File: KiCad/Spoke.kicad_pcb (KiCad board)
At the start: 2 copper layers, 50 x 100 mm, 134 parts, among them J1 B2B-PH-K-S, J10 BL-A, J11 BL-C, J12 Amphenol 132289, J2 BAT+, J3 BAT-, J4 GCT USB4105/USB4110, J5 USB+, J6 USB-, J7 PLS-1x3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

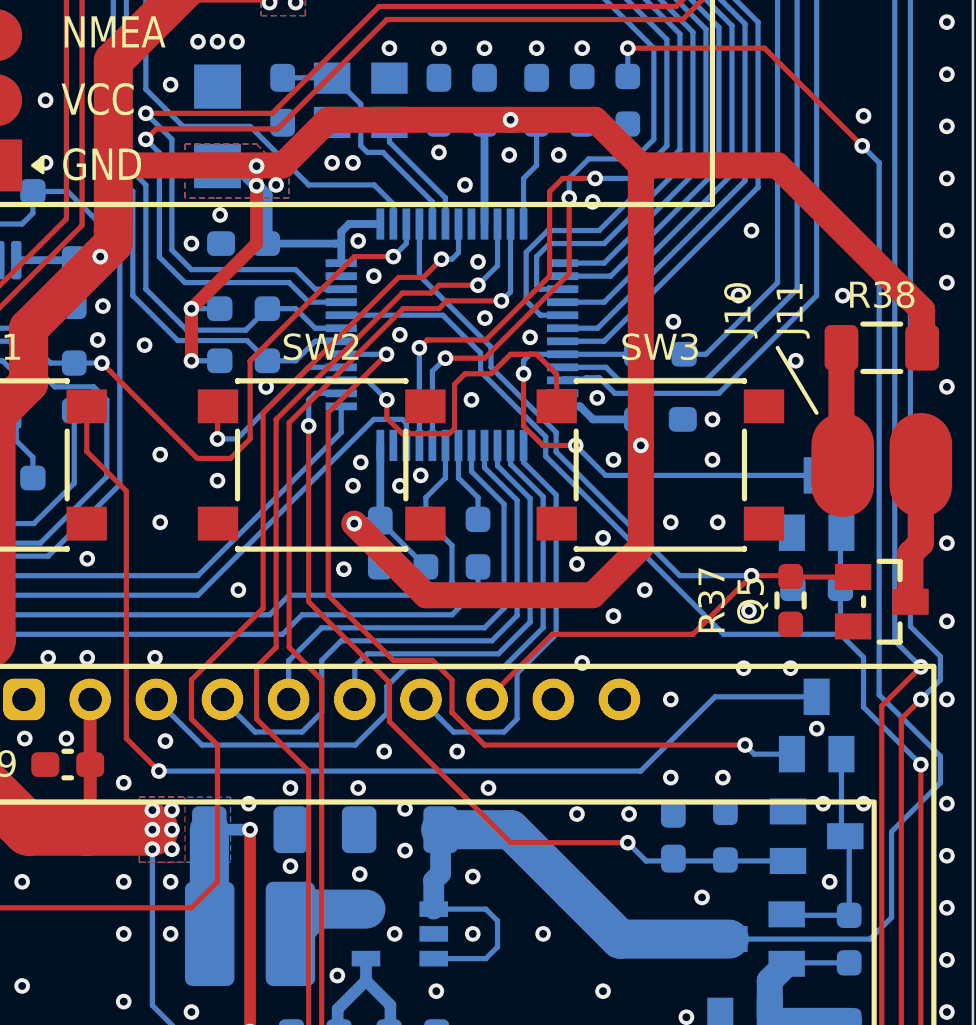
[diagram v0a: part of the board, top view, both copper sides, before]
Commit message: Swap PWR_HOLD and RF_TXEN; re-route
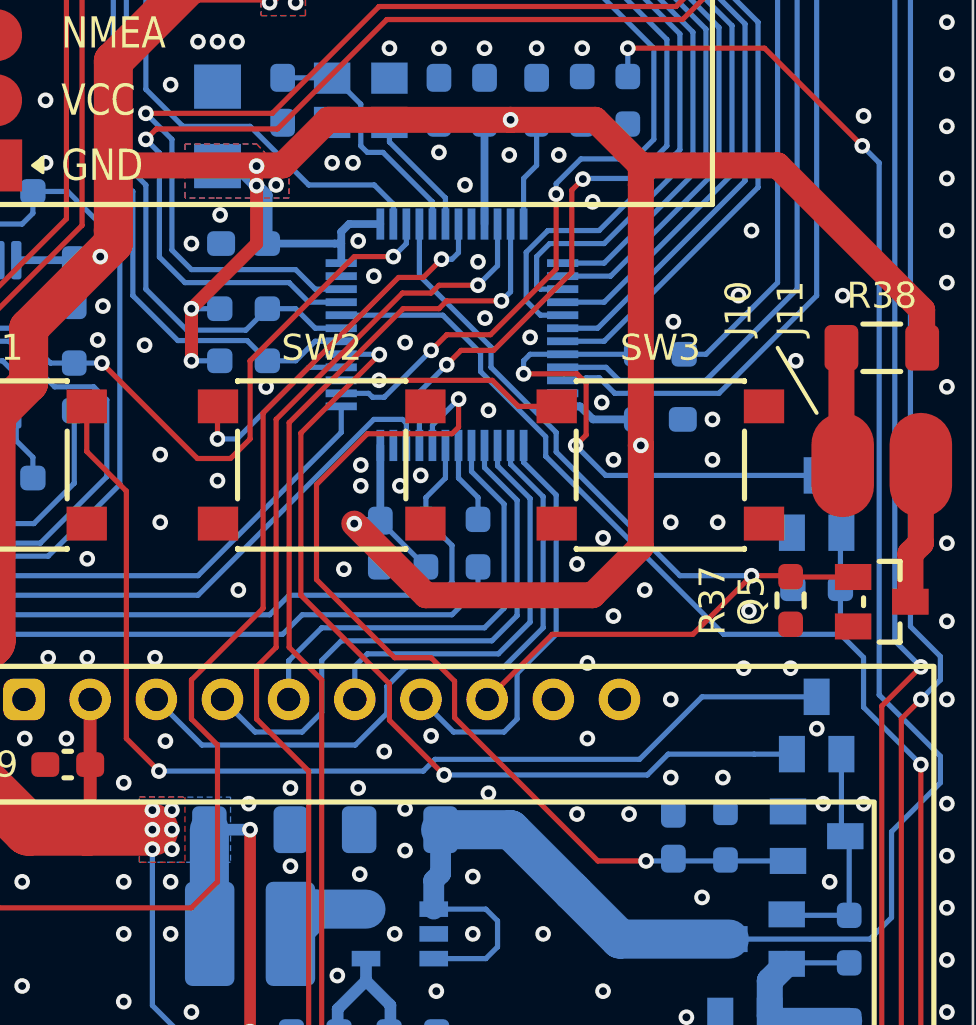
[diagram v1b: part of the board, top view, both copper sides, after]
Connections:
- U6 pad 32: RF_TXEN -> PWR_HOLD
- U6 pad 38: PWR_HOLD -> RF_TXEN
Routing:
- net BTN_ESC: track 13.3 -> 8.68 mm
- net PWR_HOLD: track 32.5 -> 36.7 mm
- net BTN_PWR: track 33.0 -> 34.8 mm
- net RF_RXEN: track 37.6 -> 36.6 mm
- net RF_TXEN: track 36.9 -> 37.8 mm
- net PPS_BOOT1: track 19.0 -> 19.8 mm
- net GND: vias 427 -> 428

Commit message: Improve PPS_BOOT1 routing
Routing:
- net PPS_BOOT1: track 19.8 -> 14.3 mm
- net GND: vias 428 -> 432
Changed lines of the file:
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@@
 	)
 	(via
+		(at 118.2 99)
+		(size 0.6)
+		(drill 0.3)
+		(layers "F.Cu" "B.Cu")
+		(free yes)
+		(net 1)
+	)
+	(via
 		(at 105 72.8)
 		(size 0.6)
@@
 	)
 	(via
-		(at 111.2 99.8)
+		(at 111 100)
 		(size 0.6)
 		(drill 0.3)
@@
 	)
 	(via
+		(at 118.8 97)
+		(size 0.6)
+		(drill 0.3)
+		(layers "F.Cu" "B.Cu")
+		(free yes)
+		(net 1)
+	)
+	(via
 		(at 100.4 88.4)
 		(size 0.6)
@@
 	)
 	(via
-		(at 113.5 94.5)
+		(at 113.6 93.6)
 		(size 0.6)
 		(drill 0.3)
@@
 	)
 	(via
-		(at 118.2 96)
+		(at 117.8 96)
 		(size 0.6)
 		(drill 0.3)
@@
 	)
 	(via
+		(at 110.1 99.2)
+		(size 0.6)
+		(drill 0.3)
+		(layers "F.Cu" "B.Cu")
+		(free yes)
+		(net 1)
+	)
+	(via
 		(at 110.751473 97.6)
 		(size 0.6)
@@
 	)
 	(via
+		(at 108 96.5)
+		(size 0.6)
+		(drill 0.3)
+		(layers "F.Cu" "B.Cu")
+		(free yes)
+		(net 1)
+	)
+	(via
 		(at 106.4 112.6)
 		(size 0.6)
@@
 	)
 	(segment
-		(start 110.150473 98.849527)
-		(end 109.75 99.25)
-		(width 0.2)
-		(layer "F.Cu")
-		(net 47)
-	)
-	(segment
-		(start 107.75 96.5)
-		(end 109.797 96.5)
+		(start 113.9 94.5)
+		(end 115.1 94.5)
 		(width 0.2)
 		(layer "F.Cu")
@@
 	)
 	(segment
-		(start 110.150473 96.853473)
-		(end 110.150473 98.849527)
-		(width 0.2)
-		(layer "F.Cu")
-		(net 47)
-	)
-	(segment
-		(start 109.797 96.5)
-		(end 110.150473 96.853473)
+		(start 115.1 94.5)
+		(end 117 96.4)
 		(width 0.2)
 		(layer "F.Cu")
@@
 	)
 	(via
-		(at 109.75 99.25)
+		(at 113.9 94.5)
 		(size 0.6)
 		(drill 0.3)
@@
 	)
 	(via
-		(at 107.75 96.5)
+		(at 117 96.4)
 		(size 0.6)
 		(drill 0.3)
@@
 	)
 	(segment
-		(start 109.75 99.25)
-		(end 110.9 100.4)
+		(start 109.25 95.75)
+		(end 112.0875 95.75)
 		(width 0.2)
 		(layer "B.Cu")
@@
 	)
 	(segment
-		(start 110.9 100.4)
-		(end 119 100.4)
+		(start 113.9 94.5)
+		(end 112.6 94.5)
 		(width 0.2)
 		(layer "B.Cu")
@@
 	)
 	(segment
-		(start 109.25 95.75)
-		(end 112.0875 95.75)
+		(start 112.6 94.5)
+		(end 112.0875 95.0125)
 		(width 0.2)
 		(layer "B.Cu")
@@
 	)
 	(segment
-		(start 108 95.75)
-		(end 109.25 95.75)
+		(start 119 100.4)
+		(end 119 98.4)
 		(width 0.2)
 		(layer "B.Cu")
@@
 	)
 	(segment
-		(start 107.75 96.5)
-		(end 107.75 96)
+		(start 119 98.4)
+		(end 117 96.4)
 		(width 0.2)
 		(layer "B.Cu")
@@
 	)
 	(segment
-		(start 107.75 96)
-		(end 108 95.75)
+		(start 112.0875 95.0125)
+		(end 112.0875 95.75)
 		(width 0.2)
 		(layer "B.Cu")

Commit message: Minor gloss
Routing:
- net GND: vias 432 -> 434

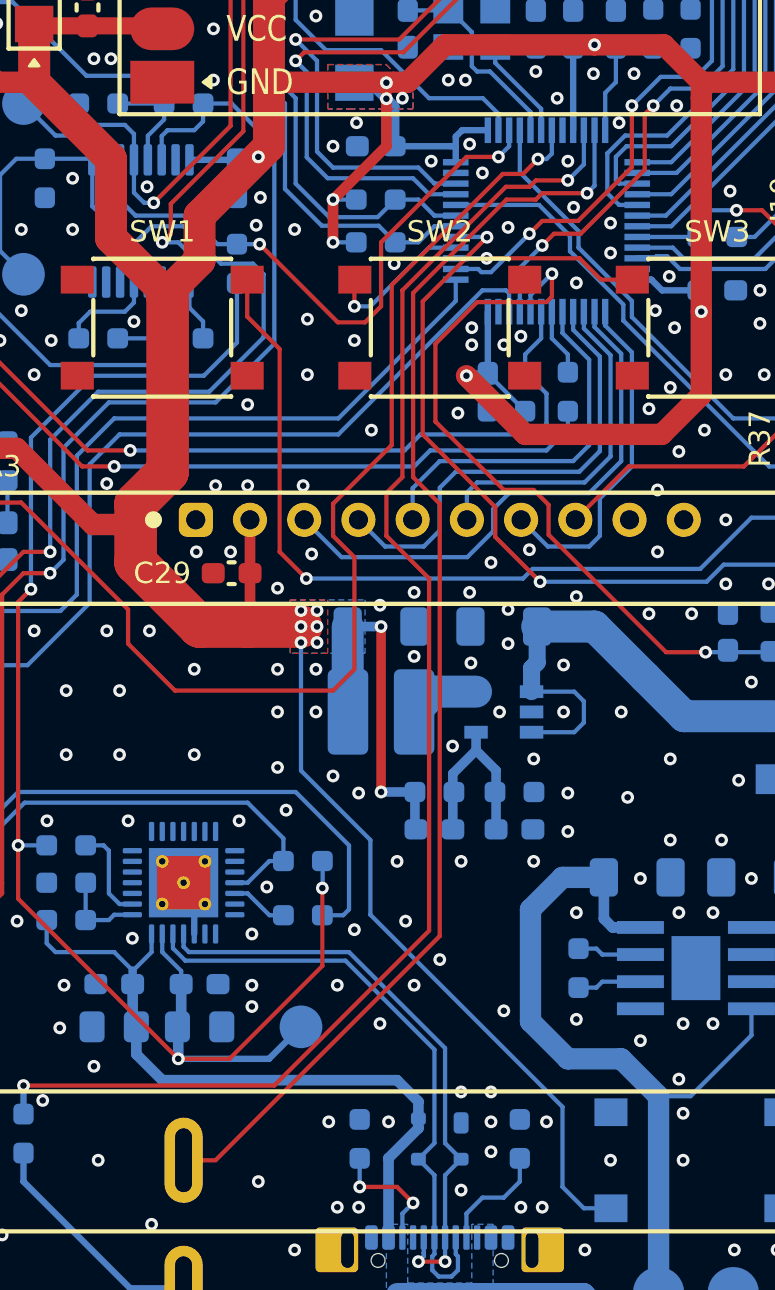
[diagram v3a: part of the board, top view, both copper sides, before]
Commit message: Move LCD_BL to PA1 (ex BUZZER_N)
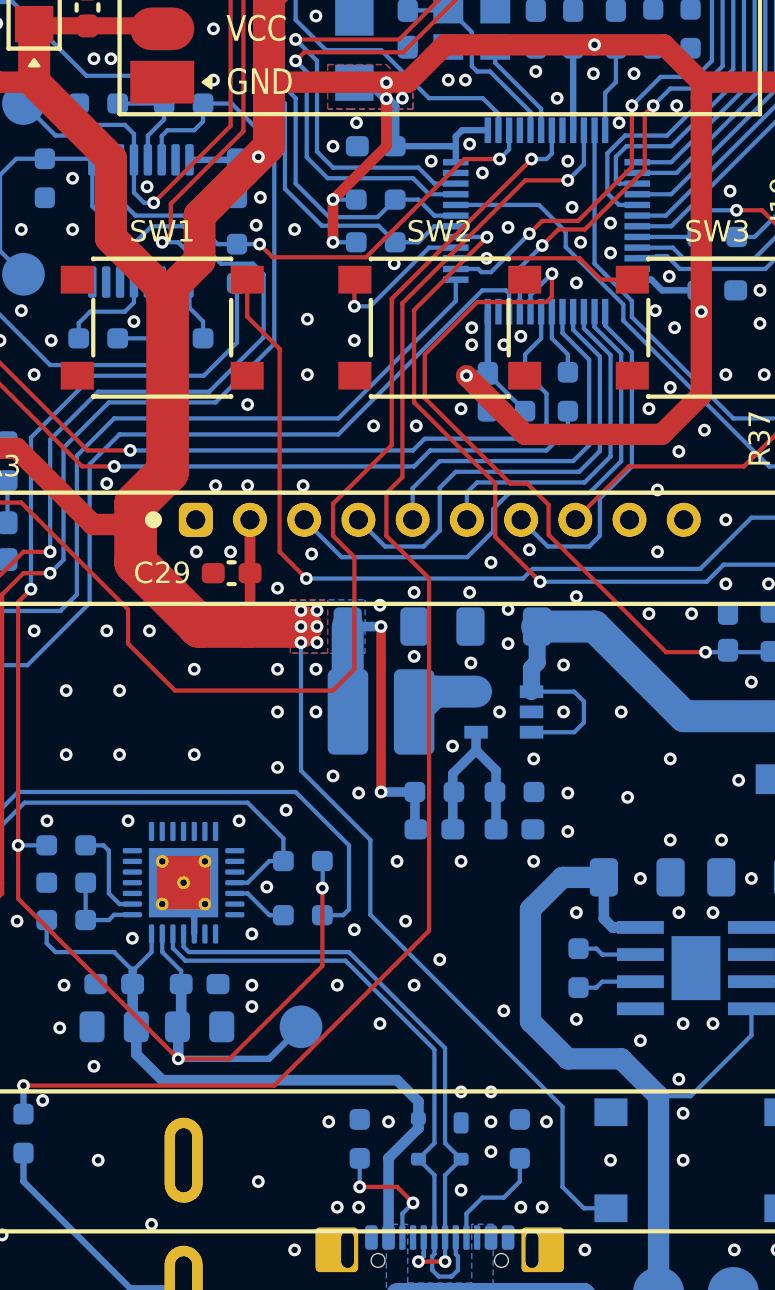
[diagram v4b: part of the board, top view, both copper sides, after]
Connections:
- net BUZZER_P renamed BUZZER
- LS1 pad 2: BUZZER_N -> unconnected-(LS1-Pad2)
- U6 pad 11: BUZZER_N -> LCD_BL
- U6 pad 4: LCD_BL -> unconnected-(U6-PC15-Pad4)
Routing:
- net BUZZER_N: track 60.2 -> 0.00 mm, vias 1 -> 0
- net MUX_BLE_USB: track 66.8 -> 62.6 mm
- net LCD_BL: track 36.4 -> 35.0 mm
- net GND: vias 434 -> 436

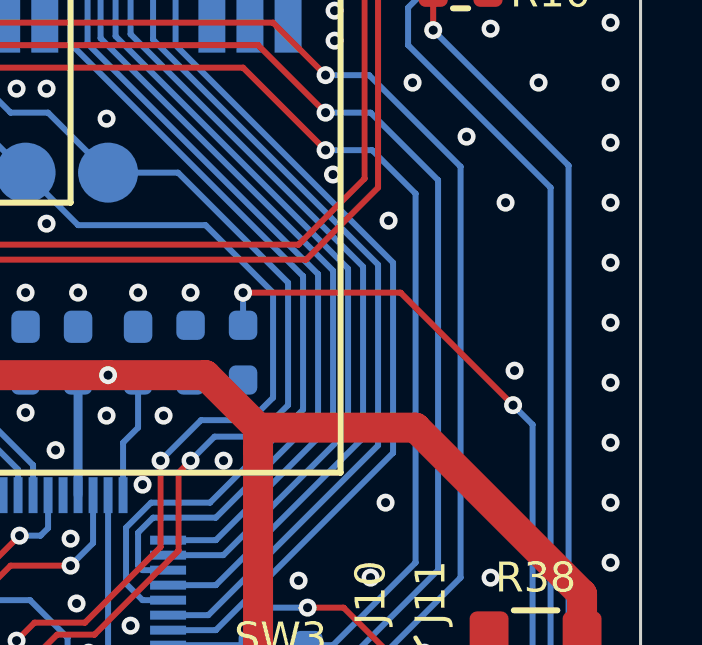
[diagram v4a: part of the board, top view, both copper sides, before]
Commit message: Add ALARM button
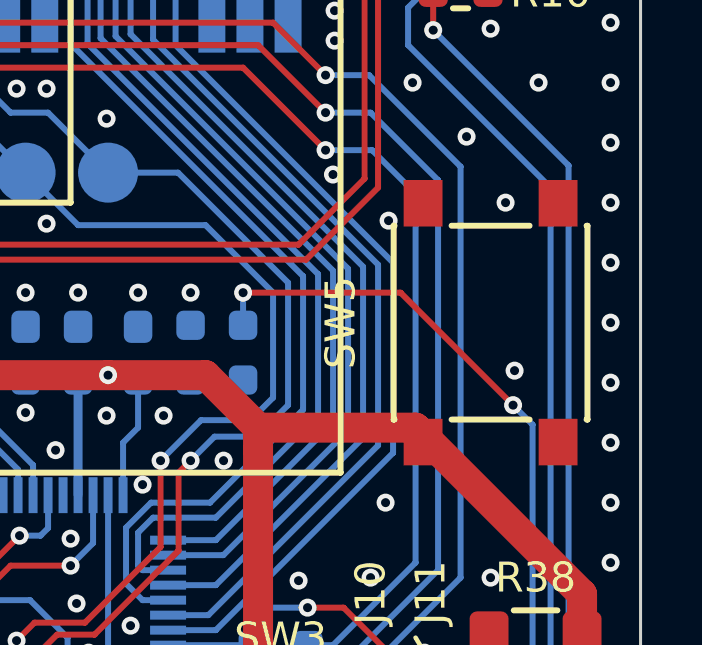
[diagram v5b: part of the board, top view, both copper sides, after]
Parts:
- added SW5: ~, Spoke:Button_6x6, F.Cu at (120.0, 85.0)
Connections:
- U6 pad 4: unconnected-(U6-PC15-Pad4) -> BTN_ALARM

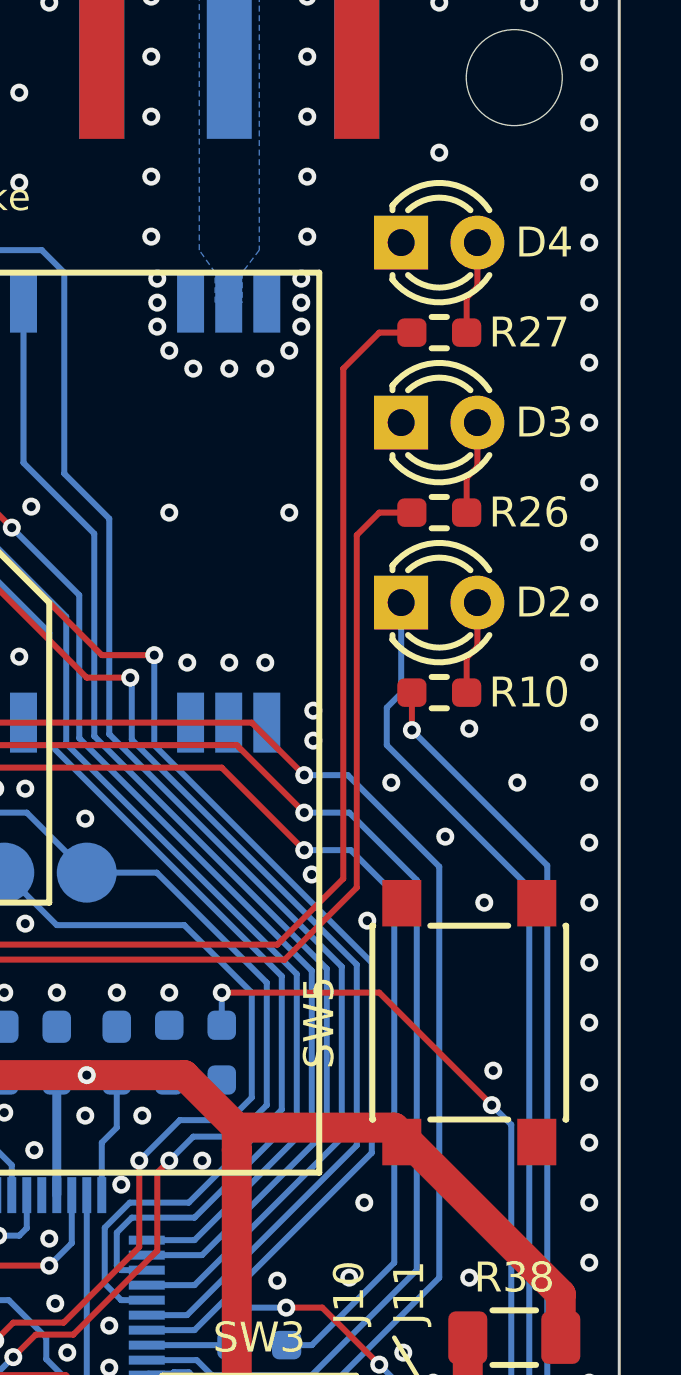
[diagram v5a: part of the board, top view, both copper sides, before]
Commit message: Tentatively move LEDs and ALARM button
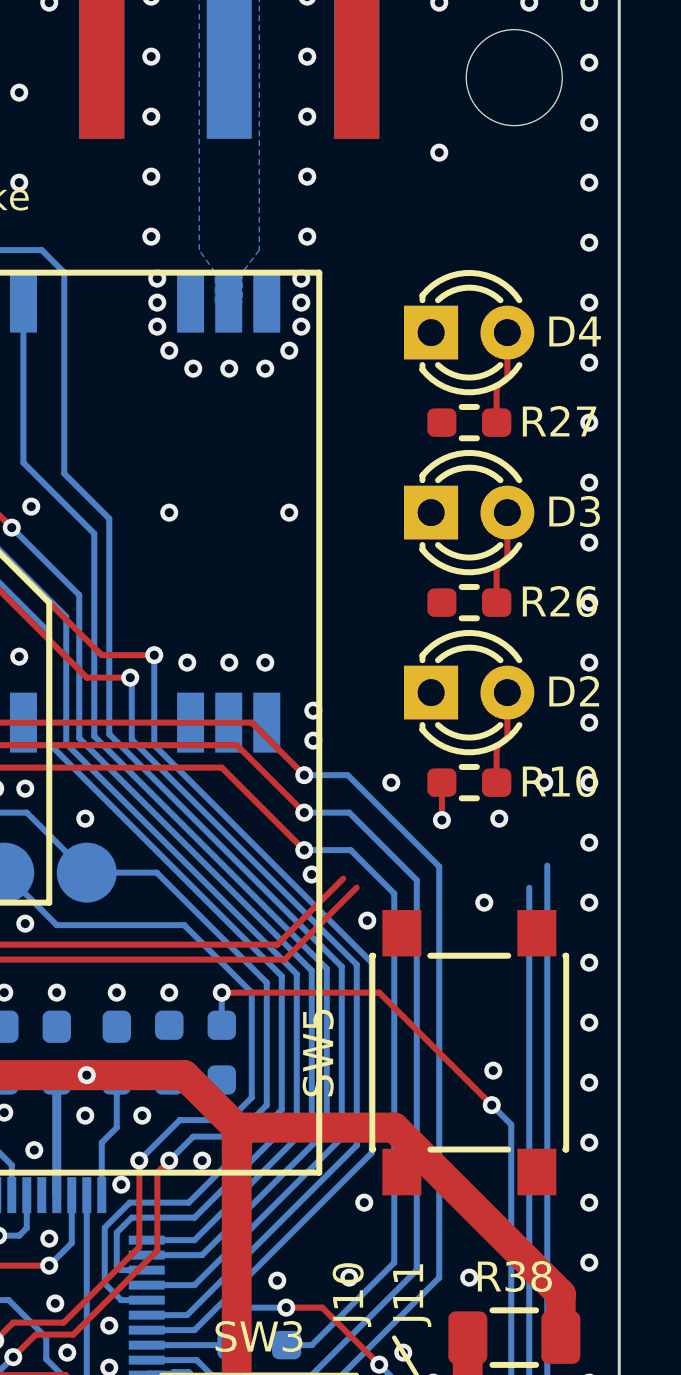
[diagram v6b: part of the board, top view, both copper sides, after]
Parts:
- moved D2 3.16 mm to (120.0, 74.0)
- moved D3 3.16 mm to (120.0, 68.0)
- moved D4 3.16 mm to (120.0, 62.0)
- moved R10 3.16 mm to (120.0, 77.0)
- moved R26 3.16 mm to (120.0, 71.0)
- moved R27 3.16 mm to (120.0, 65.0)
- moved SW5 1.00 mm to (120.0, 86.0)
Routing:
- net LED_GREEN: track 57.7 -> 37.9 mm
- net LED_RED: track 52.2 -> 38.3 mm
- net Net-(D2-K): track 68.7 -> 57.1 mm
- net VBUS: track 151.2 -> 144.8 mm
- net GND: vias 436 -> 435
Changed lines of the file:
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@@
 	(footprint "Spoke:Button_6x6"
 		(layer "F.Cu")
-		(at 120 85 90)
+		(at 120 86 90)
 		(property "Reference" "SW5"
 			(at 0 -5 90)
@@
 		(locked yes)
 		(layer "F.Cu")
-		(at 119 65)
+		(at 120 68)
 		(property "Reference" "D3"
 			(at 3.5 0 0)
@@
 		(locked yes)
 		(layer "F.Cu")
-		(at 119 71)
+		(at 120 74)
 		(property "Reference" "D2"
 			(at 3.5 0 0)
@@
 		(locked yes)
 		(layer "F.Cu")
-		(at 119 74 180)
+		(at 120 77 180)
 		(property "Reference" "R10"
 			(at -3 0 0)
@@
 		(locked yes)
 		(layer "F.Cu")
-		(at 119 59)
+		(at 120 62)
 		(property "Reference" "D4"
 			(at 3.5 0 0)
@@
 		(locked yes)
 		(layer "F.Cu")
-		(at 119 62)
+		(at 120 65)
 		(property "Reference" "R27"
 			(at 3 0 0)
@@
 		(locked yes)
 		(layer "F.Cu")
-		(at 119 68)
+		(at 120 71)
 		(property "Reference" "R26"
 			(at 3 0 0)
@@
 	)
 	(via
-		(at 119.2 78.8)
-		(size 0.6)
-		(drill 0.3)
-		(layers "F.Cu" "B.Cu")
-		(free yes)
-		(net 1)
-	)
-	(via
 		(at 111 100)
 		(size 0.6)
@@
 	)
 	(via
-		(at 121.6 77)
+		(at 122.5 77)
 		(size 0.6)
 		(drill 0.3)
@@
 	)
 	(via
-		(at 120 75.2)
+		(at 121 78.2)
 		(size 0.6)
 		(drill 0.3)
@@
 	)
 	(segment
-		(start 118.0875 75.25)
-		(end 118.0875 74)
+		(start 119.0875 78.25)
+		(end 119.0875 77)
 		(width 0.2)
 		(layer "F.Cu")
@@
 	)
 	(via
-		(at 118.0875 75.25)
+		(at 119.0875 78.25)
 		(size 0.6)
 		(drill 0.3)
@@
 	)
 	(segment
-		(start 122.6 79.7625)
-		(end 118.0875 75.25)
-		(width 0.2)
-		(layer "B.Cu")
-		(net 6)
-	)
-	(segment
 		(start 84.75 129.25)
 		(end 82 129.25)
@@
 	)
 	(segment
-		(start 116.25 80.5)
-		(end 116.25 68.75)
-		(width 0.2)
-		(layer "F.Cu")
-		(net 10)
-	)
-	(segment
 		(start 98.3 87.1)
 		(end 102.5 82.9)
@@
 	)
 	(segment
-		(start 116.25 68.75)
-		(end 117 68)
-		(width 0.2)
-		(layer "F.Cu")
-		(net 10)
-	)
-	(segment
-		(start 117 68)
-		(end 118.0875 68)
-		(width 0.2)
-		(layer "F.Cu")
-		(net 10)
-	)
-	(segment
 		(start 93.25 87.5)
 		(end 93.65 87.1)
@@
 	)
 	(segment
-		(start 115.8 63.2)
-		(end 117 62)
-		(width 0.2)
-		(layer "F.Cu")
-		(net 11)
-	)
-	(segment
-		(start 115.8 80.2)
-		(end 115.8 63.2)
-		(width 0.2)
-		(layer "F.Cu")
-		(net 11)
-	)
-	(segment
 		(start 102.2 82.4)
 		(end 113.6 82.4)
@@
 	)
 	(segment
-		(start 117 62)
-		(end 118.0875 62)
-		(width 0.2)
-		(layer "F.Cu")
-		(net 11)
-	)
-	(segment
 		(start 98.1 86.5)
 		(end 102.2 82.4)
@@
 	)
 	(segment
-		(start 120.27 72.48)
-		(end 119.9125 72.8375)
+		(start 121.27 75.48)
+		(end 120.9125 75.8375)
 		(width 0.2)
 		(layer "F.Cu")
@@
 	)
 	(segment
-		(start 120.27 71)
-		(end 120.27 72.48)
+		(start 121.27 74)
+		(end 121.27 75.48)
 		(width 0.2)
 		(layer "F.Cu")
@@
 	)
 	(segment
-		(start 119.9125 72.8375)
-		(end 119.9125 74)
+		(start 120.9125 75.8375)
+		(end 120.9125 77)
 		(width 0.2)
 		(layer "F.Cu")
@@
 	)
 	(segment
-		(start 120.27 65)
-		(end 120.27 66.48)
+		(start 121.27 68)
+		(end 121.27 69.48)
 		(width 0.2)
 		(layer "F.Cu")
@@
 	)
 	(segment
-		(start 119.9125 66.8375)
-		(end 119.9125 68)
+		(start 120.9125 69.8375)
+		(end 120.9125 71)
 		(width 0.2)
 		(layer "F.Cu")
@@
 	)
 	(segment
-		(start 120.27 66.48)
-		(end 119.9125 66.8375)
+		(start 121.27 69.48)
+		(end 120.9125 69.8375)
 		(width 0.2)
 		(layer "F.Cu")
@@
 	)
 	(segment
-		(start 119.9125 60.8375)
-		(end 119.9125 62)
+		(start 120.9125 63.8375)
+		(end 120.9125 65)
 		(width 0.2)
 		(layer "F.Cu")
@@
 	)
 	(segment
-		(start 120.27 59)
-		(end 120.27 60.48)
+		(start 121.27 62)
+		(end 121.27 63.48)
 		(width 0.2)
 		(layer "F.Cu")
@@
 	)
 	(segment
-		(start 120.27 60.48)
-		(end 119.9125 60.8375)
+		(start 121.27 63.48)
+		(end 120.9125 63.8375)
 		(width 0.2)
 		(layer "F.Cu")
@@
 	)
 	(segment
-		(start 117.25 75.75)
-		(end 117.25 74.5)
-		(width 0.2)
-		(layer "B.Cu")
-		(net 74)
-	)
-	(segment
 		(start 122 106.75)
 		(end 122 80.5)
@@
 		(width 0.2)
 		(layer "B.Cu")
-		(net 74)
-	)
-	(segment
-		(start 117.73 74.02)
-		(end 117.73 71)
-		(width 0.2)
-		(layer "B.Cu")
-		(net 74)
-	)
-	(segment
-		(start 122 80.5)
-		(end 117.25 75.75)
-		(width 0.2)
-		(layer "B.Cu")
-		(net 74)
-	)
-	(segment
-		(start 117.25 74.5)
-		(end 117.73 74.02)
-		(width 0.2)
-		(layer "B.Cu")
